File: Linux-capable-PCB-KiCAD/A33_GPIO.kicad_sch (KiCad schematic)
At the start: 44 parts

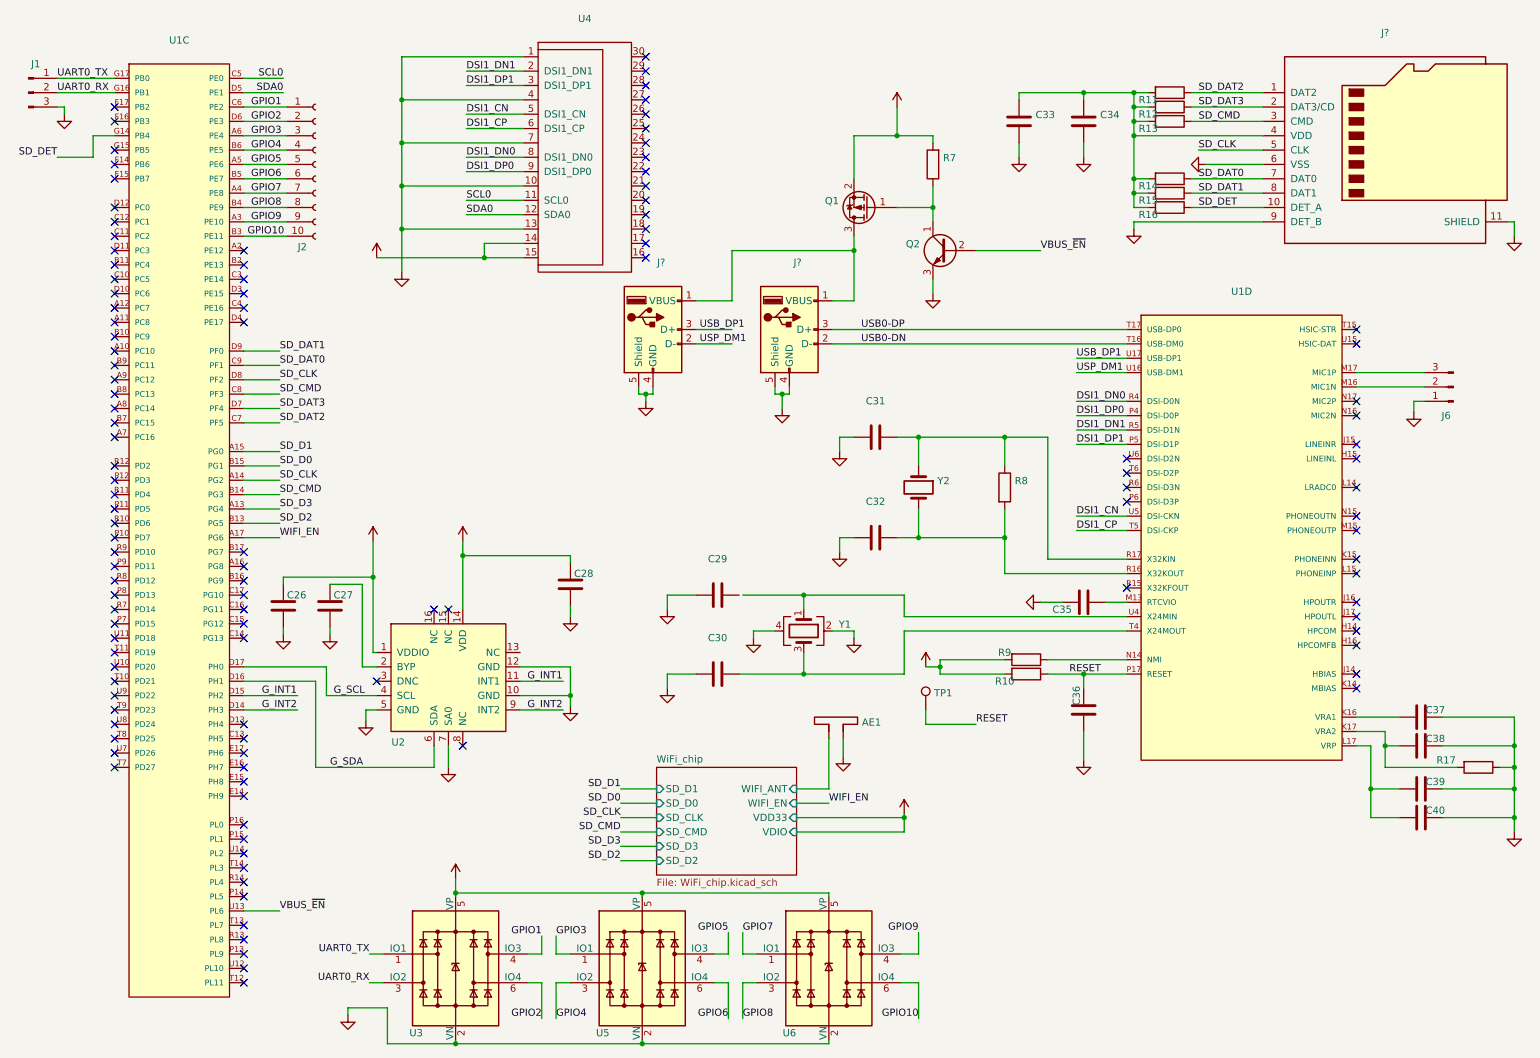
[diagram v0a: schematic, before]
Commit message: Dodao 3.3V na SD karticu, treba zamjeniti SD konektor, zavrsio napjanje, treba izracunati vrijednosti otpornika i footprint preci za komponente
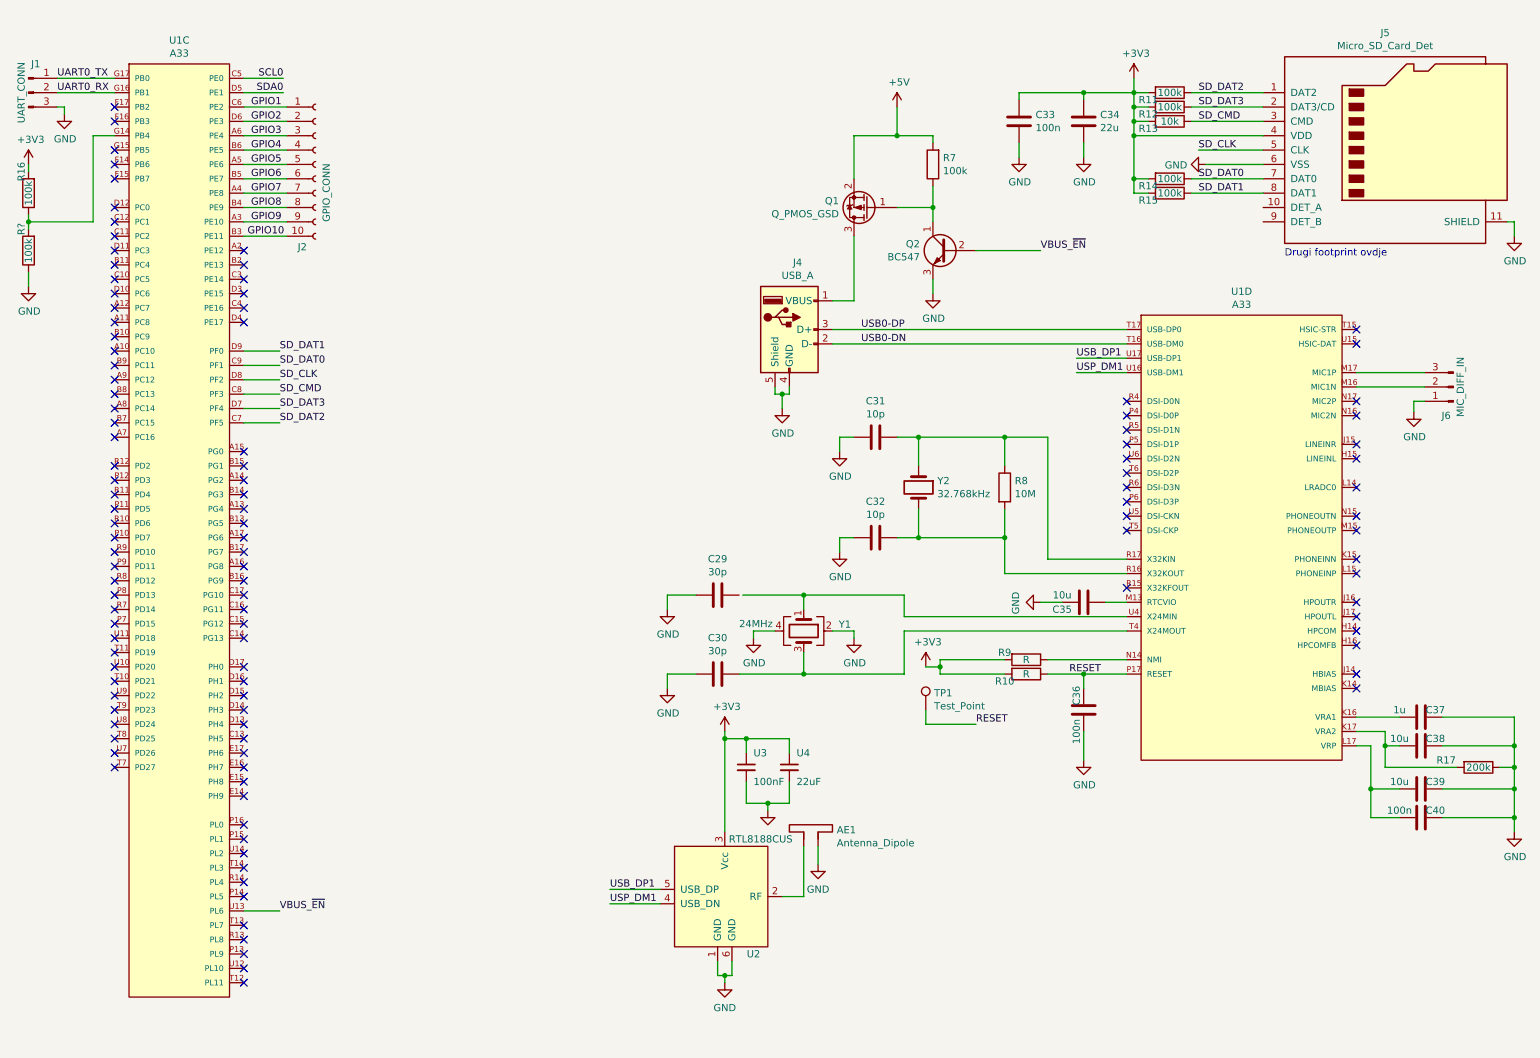
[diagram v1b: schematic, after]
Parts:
- removed C26, C27, C28: (no value), symbol Linux-capable-PCB-KiCAD-rescue:C-Device
- removed J?: (no value), symbol Linux-capable-PCB-KiCAD-rescue:USB_A-Connector
- removed U2: (no value), symbol MMA8425Q_Gsensor:MMA8425Q_Gsensor
- removed U3, U5, U6: (no value), symbol Linux-capable-PCB-KiCAD-rescue:SRV05-4-Power_Protection
- removed U4: (no value), symbol MIPI_DSI_Raspberry:MIPI_DSI_Raspberry
- added R?: 100k, Resistor_SMD:R_0603_1608Metric, symbol Linux-capable-PCB-KiCAD-rescue:R-device
- added U2: RTL8188CUS, realtek:RTL8188CUS, symbol realtek:RTL8188CUS
- added U3: 100nF, Capacitor_SMD:C_0402_1005Metric, symbol hardware-rescue:C_Small-Device
- added U4: 22uF, Capacitor_SMD:C_0402_1005Metric, symbol hardware-rescue:C_Small-Device
- AE1: value (none) -> Antenna_Dipole; footprint (none) -> Small2_4GHz_PCB_Antenna:Small2_4GHz_PCB_Antenna
- C29, C30: value (none) -> 30p; footprint (none) -> Capacitor_SMD:C_0603_1608Metric
- C31, C32: value (none) -> 10p; footprint (none) -> Capacitor_SMD:C_0603_1608Metric
- C33, C36, C40: value (none) -> 100n; footprint (none) -> Capacitor_SMD:C_0603_1608Metric
- C34: value (none) -> 22u; footprint (none) -> Capacitor_SMD:C_0603_1608Metric
- C35, C38, C39: value (none) -> 10u; footprint (none) -> Capacitor_SMD:C_0603_1608Metric
- C37: value (none) -> 1u; footprint (none) -> Capacitor_SMD:C_0603_1608Metric
- J1: value (none) -> UART_CONN; footprint (none) -> Connector_PinHeader_2.54mm:PinHeader_1x03_P2.54mm_Vertical
- J2: value (none) -> GPIO_CONN; footprint (none) -> Connector_PinHeader_2.54mm:PinHeader_1x10_P2.54mm_Vertical
- J4: renamed from J?; value (none) -> USB_A; footprint (none) -> Connector_USB:USB_Micro-B_Molex-105017-0001
- J5: renamed from J?; value (none) -> Micro_SD_Card_Det; footprint (none) -> Connector_Card:microSD_HC_Molex_104031-0811
- J6: value (none) -> MIC_DIFF_IN; footprint (none) -> Connector_PinSocket_2.54mm:PinSocket_1x03_P2.54mm_Vertical
- Q1: value (none) -> Q_PMOS_GSD
- Q2: value (none) -> BC547; footprint (none) -> TO_SOT_Packages_THT:TO-92_Molded_Narrow
- R10, R9: value (none) -> R; footprint (none) -> Resistor_SMD:R_0603_1608Metric
- R11, R12, R14, R15, R16, R7: value (none) -> 100k; footprint (none) -> Resistor_SMD:R_0603_1608Metric
- R13: value (none) -> 10k; footprint (none) -> Resistor_SMD:R_0603_1608Metric
- R17: value (none) -> 200k; footprint (none) -> Resistor_SMD:R_0603_1608Metric
- R8: value (none) -> 10M; footprint (none) -> Resistor_SMD:R_0603_1608Metric
- TP1: value (none) -> Test_Point; footprint (none) -> TestPoint:TestPoint_Pad_1.0x1.0mm
- U1: value (none) -> A33; footprint (none) -> eec:Allwinner_Technology_Co.,_Ltd.-A33-0
- Y1: value (none) -> 24MHz; footprint (none) -> Crystal:Crystal_SMD_EuroQuartz_MJ-4Pin_5.0x3.2mm
- Y2: value (none) -> 32.768kHz; footprint (none) -> Crystal:Crystal_SMD_EuroQuartz_MJ-4Pin_5.0x3.2mm
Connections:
- net +3V3: now also C33.1, C34.1, J5.4 (VDD), R11.2, R12.2, R13.2, R14.2, R15.2, R16.2, U2.3 (Vcc), U3.1, U4.1
- net GND: now also R?.1, U2.1 (GND), U2.6 (GND), U3.2, U4.2; no longer J5.9 (DET_B)
- net SD_CLK: no longer U1.A14 (PG2)
- net SD_CMD: no longer U1.B14 (PG3)
- net USB_DP1: now also U2.5 (USB_DP)
- net USP_DM1: now also U2.4 (USB_DN)
- net DSI1_CN: no longer names the net of U1.U5 (DSI-CKN)
- net DSI1_CP: no longer names the net of U1.T5 (DSI-CKP)
- net DSI1_DN0: no longer names the net of U1.R4 (DSI-D0N)
- net DSI1_DN1: no longer names the net of U1.R5 (DSI-D1N)
- net DSI1_DP0: no longer names the net of U1.P4 (DSI-D0P)
- net DSI1_DP1: no longer names the net of U1.P5 (DSI-D1P)
- net G_INT1: no longer names the net of U1.D15 (PH2)
- net G_INT2: no longer names the net of U1.D14 (PH3)
- net G_SCL: no longer names the net of U1.D17 (PH0)
- net G_SDA: no longer names the net of U1.D16 (PH1)
- net SD_D0: no longer names the net of U1.B15 (PG1)
- net SD_D1: no longer names the net of U1.A15 (PG0)
- net SD_D2: no longer names the net of U1.B13 (PG5)
- net SD_D3: no longer names the net of U1.A13 (PG4)
- net SD_DET: no longer names the net of R16.1, U1.G14 (PB4)
- net SD_DET: now also R?.2; no longer J5.10 (DET_A)
- net WIFI_EN: no longer names the net of U1.A17 (PG6)
- net WiFi_chip/WIFI_ANT: no longer names the net of AE1.1
- net WiFi_chip/WIFI_ANT: now also U2.2 (RF)
- no-connect marks 115 -> 113
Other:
- removed sheet WiFi_chip
- note added: "Drugi footprint ovdje"
- moved on the sheet: AE1, R16
